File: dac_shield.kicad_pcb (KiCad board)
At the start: 2 copper layers, 68.6 x 53.3 mm, 34 parts, among them P1 CONN_2, P2 CONN_2, P3 CONN_2, T1 VrefTest, U1 MCP4921, U2 TCA0372, U3 LM741

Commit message: Changed origin to generate gerber files
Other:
- board text added: "2016 Visgence Inc."
- board text removed: "2014 Visgence Inc."
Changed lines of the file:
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@@
     (links 59)
     (no_connects 0)
-    (area 30.416499 28.892499 99.110001 82.359501)
+    (area 27.94 25.4 101.600001 85.090001)
     (thickness 1.6)
     (drawings 78)
@@
     (pad_drill 0.9652)
     (pad_to_mask_clearance 0)
-    (aux_axis_origin 0 0)
+    (aux_axis_origin 30.48 82.296)
     (visible_elements 7FFFFBBF)
     (pcbplotparams
-      (layerselection 0x00030_80000001)
+      (layerselection 0x010f0_80000001)
       (usegerberextensions true)
       (excludeedgelayer false)
@@
       (viasonmask false)
       (mode 1)
-      (useauxorigin false)
+      (useauxorigin true)
       (hpglpennumber 1)
       (hpglpenspeed 20)
@@
     (descr "Bornier d'alimentation 2 pins")
     (tags DEV)
-    (fp_text reference P3 (at 0 -5.08 270) (layer F.SilkS)
+    (fp_text reference P3 (at 0 -5.08 270) (layer F.SilkS) hide
       (effects (font (thickness 0.3048)))
     )
@@
     (descr "Bornier d'alimentation 2 pins")
     (tags DEV)
-    (fp_text reference P1 (at 0 -5.08 270) (layer F.SilkS)
+    (fp_text reference P1 (at 0 -5.08 270) (layer F.SilkS) hide
       (effects (font (thickness 0.3048)))
     )
@@
     (descr "Bornier d'alimentation 2 pins")
     (tags DEV)
-    (fp_text reference P2 (at 0 -5.08 270) (layer F.SilkS)
+    (fp_text reference P2 (at 0 -5.08 270) (layer F.SilkS) hide
       (effects (font (thickness 0.3048)))
     )
@@
   (gr_line (start 54.356 71.12) (end 54.356 76.2) (angle 90) (layer F.SilkS) (width 0.2))
   (gr_line (start 51.816 71.12) (end 51.816 76.2) (angle 90) (layer F.SilkS) (width 0.2))
-  (gr_text "2014 Visgence Inc." (at 83.185 72.39) (layer F.SilkS)
+  (gr_text "2016 Visgence Inc." (at 83.185 72.39) (layer F.SilkS)
     (effects (font (size 1.5 1.5) (thickness 0.3)))
   )

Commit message: Changed to 2017
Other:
- board text added: "2017 Visgence Inc."
- board text removed: "2016 Visgence Inc."
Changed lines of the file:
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@@
-(kicad_pcb (version 4) (host pcbnew 4.0.2-stable)
+(kicad_pcb (version 4) (host pcbnew 4.0.6)
   (general
     (links 59)
@@
   (gr_line (start 54.356 71.12) (end 54.356 76.2) (angle 90) (layer F.SilkS) (width 0.2))
   (gr_line (start 51.816 71.12) (end 51.816 76.2) (angle 90) (layer F.SilkS) (width 0.2))
-  (gr_text "2016 Visgence Inc." (at 83.185 72.39) (layer F.SilkS)
+  (gr_text "2017 Visgence Inc." (at 83.185 72.39) (layer F.SilkS)
     (effects (font (size 1.5 1.5) (thickness 0.3)))
   )

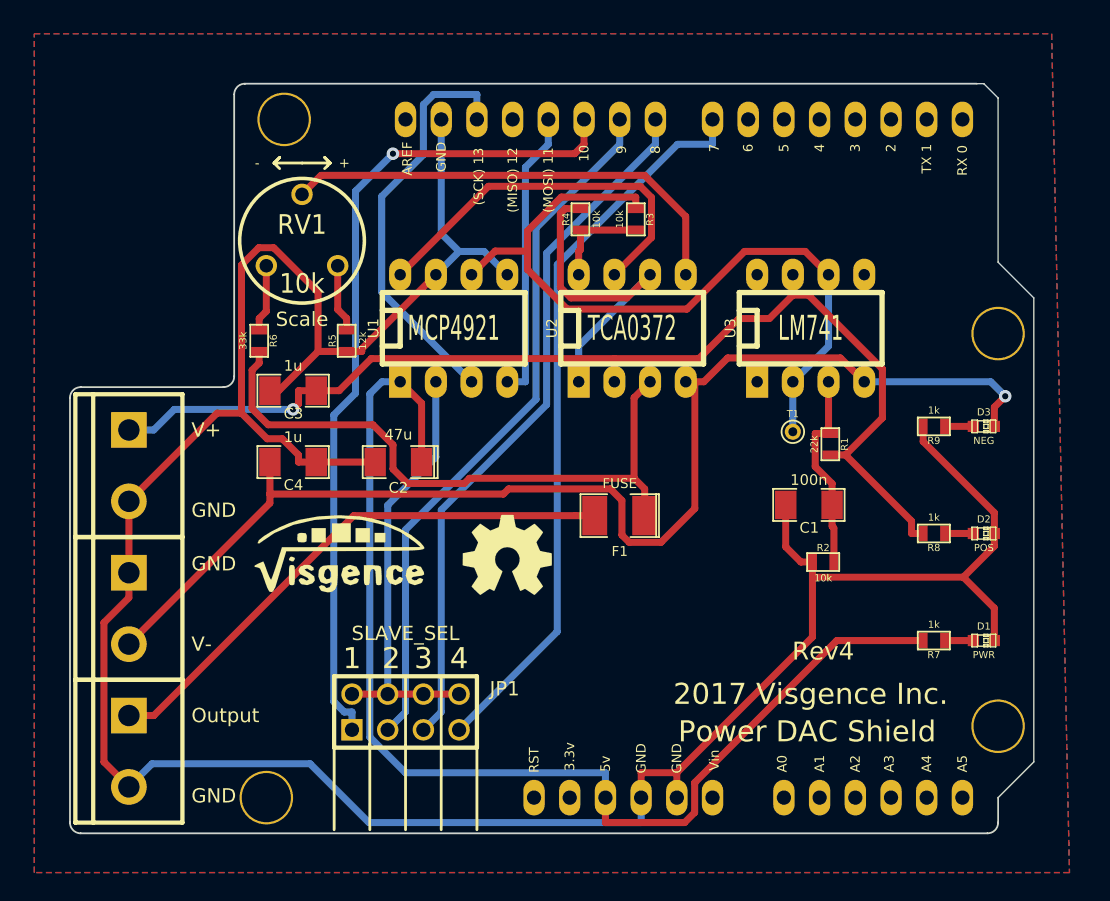
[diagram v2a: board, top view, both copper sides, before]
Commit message: Re-mapping symbols to footprints
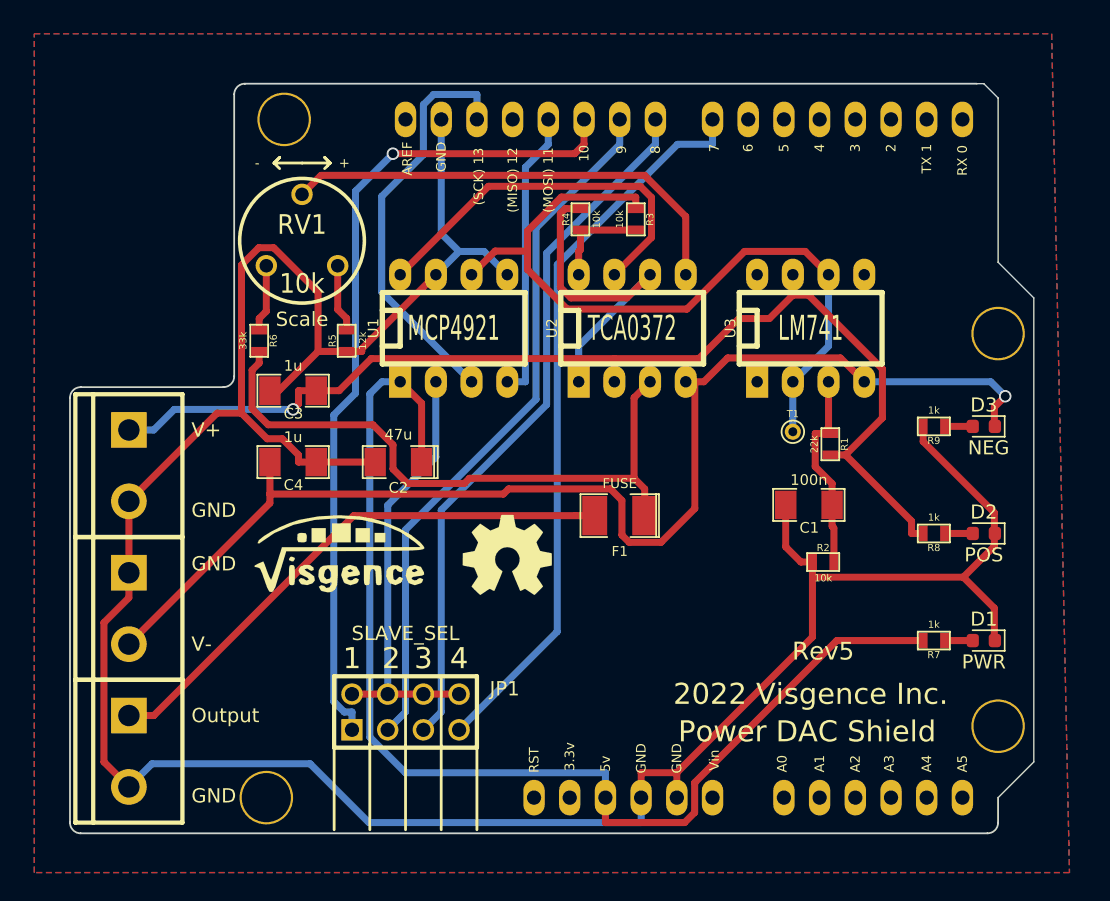
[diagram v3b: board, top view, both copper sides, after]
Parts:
- C1, C3, C4: footprint SM1206_VIS -> custom-footprints:SM1206_VIS
- C2: footprint SM1206POL_VIS -> custom-footprints:SM1206POL_VIS
- D1, D2, D3: footprint LED-0603 -> LED_SMD:LED_0603_1608Metric
- F1: footprint SM1210L -> custom-footprints:SM1210L
- G***: footprint LOGOMIRROR -> custom-footprints:LOGOMIRROR
- G1: footprint LOGO -> custom-footprints:LOGO
- G2: footprint OSHW_LOGO -> custom-footprints:OSHW_LOGO
- JP1: footprint pin_array_4x2 -> custom-footprints:pin_array_4x2
- P1, P2, P3: footprint bornier2 -> custom-footprints:bornier2
- R1, R2, R3, R4, R5, R6, R7, R8, R9: footprint SM0603_VIS -> custom-footprints:SM0603_VIS
- RV1: footprint Var_resistor -> custom-footprints:Var_resistor
- SHIELD1: footprint ARDUINO_SHIELD_2_040pins -> custom-footprints:ARDUINO_SHIELD_2_040pins
- T1: footprint PINTST -> custom-footprints:PINTST
- U1, U2, U3: footprint DIP-8__300_ELL -> custom-footprints:DIP-8__300_ELL
- h1, h2, h3, h4: footprint hole -> custom-footprints:hole
- turned D1 to 180 degrees
- turned D2 to 180 degrees
- turned D3 to 180 degrees
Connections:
- D1 pad 1: N-000002 -> GND
- D1 pad 2: GND -> Net-(D1-Pad2)
- D2 pad 1: N-000005 -> GND
- D2 pad 2: GND -> Net-(D2-Pad2)
- D3 pad 1: N-000004 -> VSS
- D3 pad 2: VSS -> Net-(D3-Pad2)
- R7 pad 1: N-000002 -> Net-(D1-Pad2)
- R8 pad 1: N-000005 -> Net-(D2-Pad2)
- R9 pad 1: N-000004 -> Net-(D3-Pad2)
- SHIELD1 pad 0: (no net) -> unconnected-(SHIELD1-Pad0)
- SHIELD1 pad 1: (no net) -> unconnected-(SHIELD1-Pad1)
- SHIELD1 pad 12: (no net) -> unconnected-(SHIELD1-Pad12)
- SHIELD1 pad 2: (no net) -> unconnected-(SHIELD1-Pad2)
- SHIELD1 pad 3: (no net) -> unconnected-(SHIELD1-Pad3)
- SHIELD1 pad 3V3: (no net) -> unconnected-(SHIELD1-Pad3V3)
- SHIELD1 pad 4: (no net) -> unconnected-(SHIELD1-Pad4)
- SHIELD1 pad 5: (no net) -> unconnected-(SHIELD1-Pad5)
- SHIELD1 pad 6: (no net) -> unconnected-(SHIELD1-Pad6)
- SHIELD1 pad AD0: (no net) -> unconnected-(SHIELD1-PadAD0)
- SHIELD1 pad AD1: (no net) -> unconnected-(SHIELD1-PadAD1)
- SHIELD1 pad AD2: (no net) -> unconnected-(SHIELD1-PadAD2)
- SHIELD1 pad AD3: (no net) -> unconnected-(SHIELD1-PadAD3)
- SHIELD1 pad AD4: (no net) -> unconnected-(SHIELD1-PadAD4)
- SHIELD1 pad AD5: (no net) -> unconnected-(SHIELD1-PadAD5)
- SHIELD1 pad AREF: (no net) -> unconnected-(SHIELD1-PadAREF)
- SHIELD1 pad RST: (no net) -> unconnected-(SHIELD1-PadRST)
- SHIELD1 pad V_IN: (no net) -> unconnected-(SHIELD1-PadV_IN)
- U3 pad 1: (no net) -> unconnected-(U3-Pad1)
- U3 pad 5: (no net) -> unconnected-(U3-Pad5)
- U3 pad 8: (no net) -> unconnected-(U3-Pad8)
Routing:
- net Net-(D3-Pad2): track 0.00 -> 2.04 mm
- net Net-(D2-Pad2): track 0.00 -> 2.04 mm
- net Net-(D1-Pad2): track 0.00 -> 2.04 mm
- net N-000005: track 2.04 -> 0.00 mm
- net N-000004: track 2.04 -> 0.00 mm
- net N-000002: track 2.04 -> 0.00 mm
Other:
- net class Default removed
- board text added: "2022 Visgence Inc."
- board text added: "Rev5"
- board text removed: "2017 Visgence Inc."
- board text removed: "Rev4"

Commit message: Got PCB mostly updated
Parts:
- R1, R2, R3, R4, R5, R6, R7, R8, R9: footprint custom-footprints:SM0603_VIS -> Resistor_SMD:R_0603_1608Metric
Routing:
- net DAC_OUT: track 27.4 -> 28.5 mm
- net Net-(RV1-Pad2): track 33.2 -> 34.0 mm

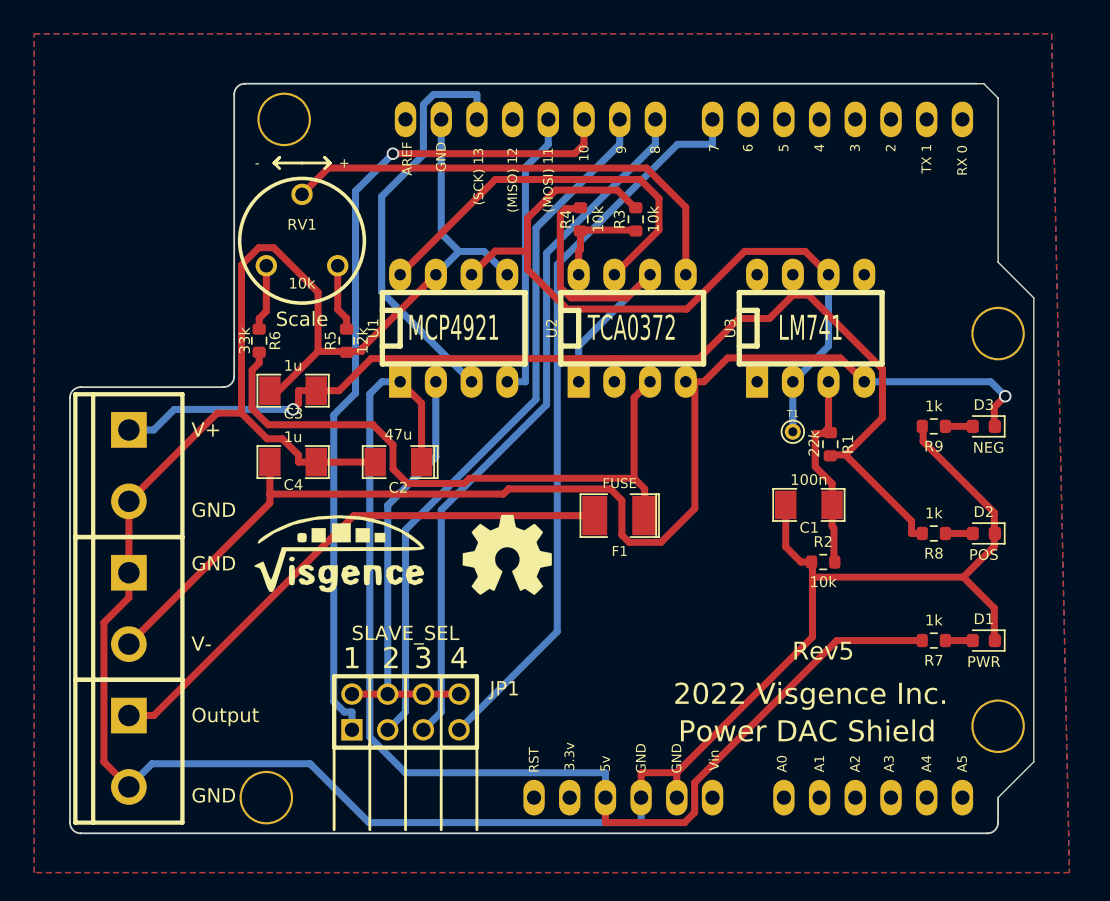
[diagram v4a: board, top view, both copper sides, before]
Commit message: Cleaning up tracks, updated led resistors
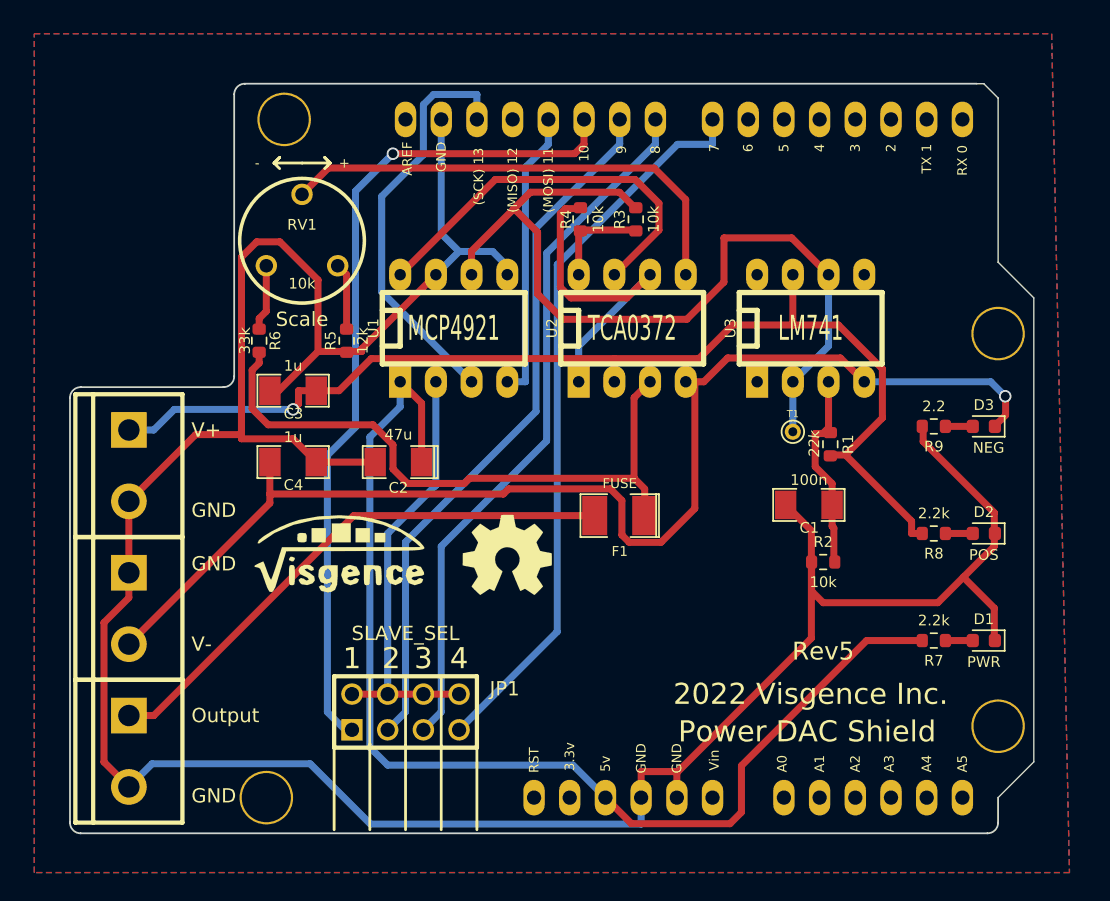
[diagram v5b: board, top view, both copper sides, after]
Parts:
- R7, R8: value 1k -> 2.2k
- R9: value 1k -> 2.2
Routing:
- net VREF: track 54.6 -> 61.3 mm
- net GND: track 198.3 -> 204.5 mm
- net +5V: track 83.9 -> 82.2 mm

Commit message: Added curved traces, updated 3d settings
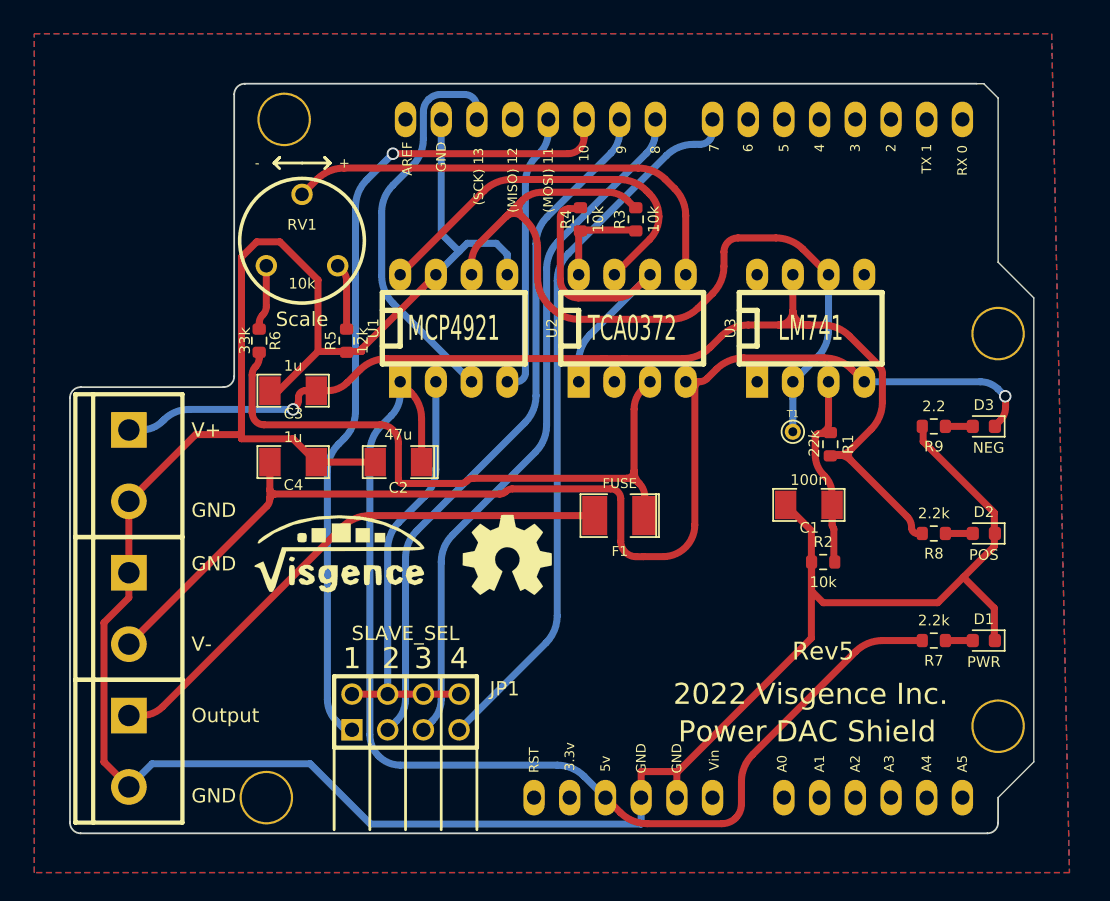
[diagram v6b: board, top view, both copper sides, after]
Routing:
- net VDD: track 80.4 -> 84.1 mm
- net VSS: track 87.6 -> 90.7 mm
- net Net-(F1-Pad1): track 45.1 -> 47.0 mm
- net +5V: track 82.2 -> 81.0 mm
- net GND: track 204.5 -> 205.5 mm
- net CLK: track 29.5 -> 28.6 mm
- net Net-(JP1-Pad7): track 52.4 -> 51.6 mm
- net Net-(JP1-Pad1): track 59.6 -> 59.0 mm
- net Net-(JP1-Pad5): track 50.3 -> 49.7 mm
- net Net-(JP1-Pad3): track 50.3 -> 49.7 mm
- net MOSI: track 20.6 -> 20.1 mm

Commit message: Removed routing and copper fill
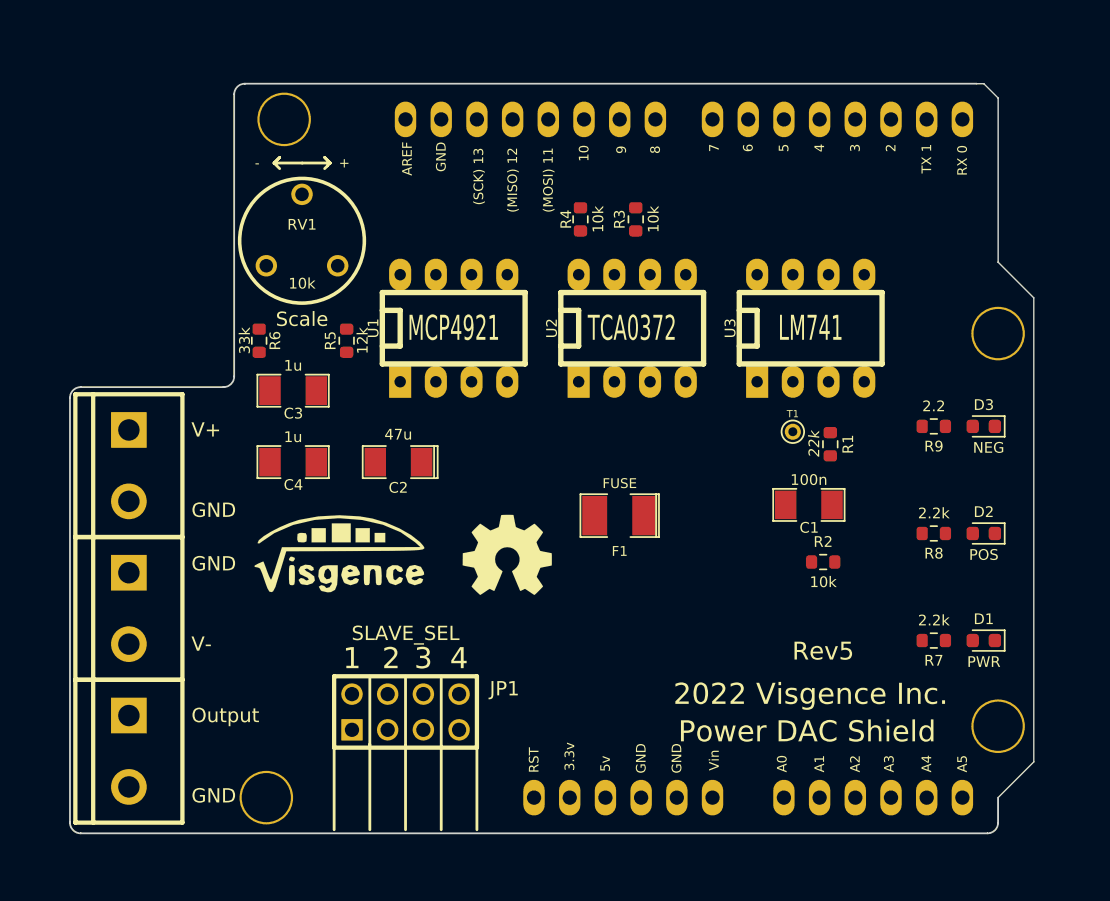
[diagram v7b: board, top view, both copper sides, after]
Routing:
- net GND: track 205.5 -> 0.00 mm
- net VSS: track 90.7 -> 0.00 mm, vias 1 -> 0
- net VDD: track 84.1 -> 0.00 mm, vias 1 -> 0
- net +5V: track 81.0 -> 0.00 mm
- net VREF: track 61.2 -> 0.00 mm
- net Net-(JP1-Pad1): track 59.0 -> 0.00 mm, vias 1 -> 0
- net Net-(JP1-Pad7): track 51.6 -> 0.00 mm
- net Net-(JP1-Pad3): track 49.7 -> 0.00 mm
- net Net-(JP1-Pad5): track 49.7 -> 0.00 mm
- net Net-(F1-Pad1): track 47.0 -> 0.00 mm
- net Net-(F1-Pad2): track 38.8 -> 0.00 mm
- net Net-(RV1-Pad2): track 34.0 -> 0.00 mm
- net Net-(JP1-Pad2): track 31.0 -> 0.00 mm
- net CLK: track 28.6 -> 0.00 mm
- net DAC_OUT: track 27.8 -> 0.00 mm
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- removed copper zone on B.Cu, net GND
- removed copper zone on F.Cu, net GND

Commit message: very routed, note extra footprint warnings
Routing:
- net VSS: track 0.00 -> 121.9 mm
- net Net-(JP1-Pad1): track 0.00 -> 104.0 mm
- net VDD: track 0.00 -> 101.3 mm
- net Net-(JP1-Pad5): track 0.00 -> 95.5 mm, vias 0 -> 1
- net Net-(JP1-Pad3): track 0.00 -> 95.1 mm
- net Net-(JP1-Pad7): track 0.00 -> 90.8 mm, vias 0 -> 1
- net +5V: track 0.00 -> 63.9 mm
- net Net-(F1-Pad2): track 0.00 -> 62.8 mm
- net Net-(F1-Pad1): track 0.00 -> 53.0 mm
- net VREF: track 0.00 -> 44.0 mm
- net Net-(C1-Pad1): track 0.00 -> 41.6 mm
- net Net-(JP1-Pad2): track 0.00 -> 38.3 mm
- net Net-(RV1-Pad2): track 0.00 -> 33.7 mm
- net CLK: track 0.00 -> 22.6 mm
- net MOSI: track 0.00 -> 20.1 mm
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- added copper zone on B.Cu, net GND
- added copper zone on F.Cu, net GND
